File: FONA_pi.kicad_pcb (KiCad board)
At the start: 2 copper layers, 88.4 x 59.1 mm, 35 parts, among them J1 Conn_01x20_Socket, J10 Conn_01x04_Pin, J11 Conn_01x20_Socket, J12 Conn_01x20_Socket, J13 Conn_01x06_Socket, J14 Conn_01x06_Socket, J15 Conn_01x06_Socket, J17 Conn_01x06_Socket, J18 Conn_01x04, J2 Conn_02x20_Odd_Even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

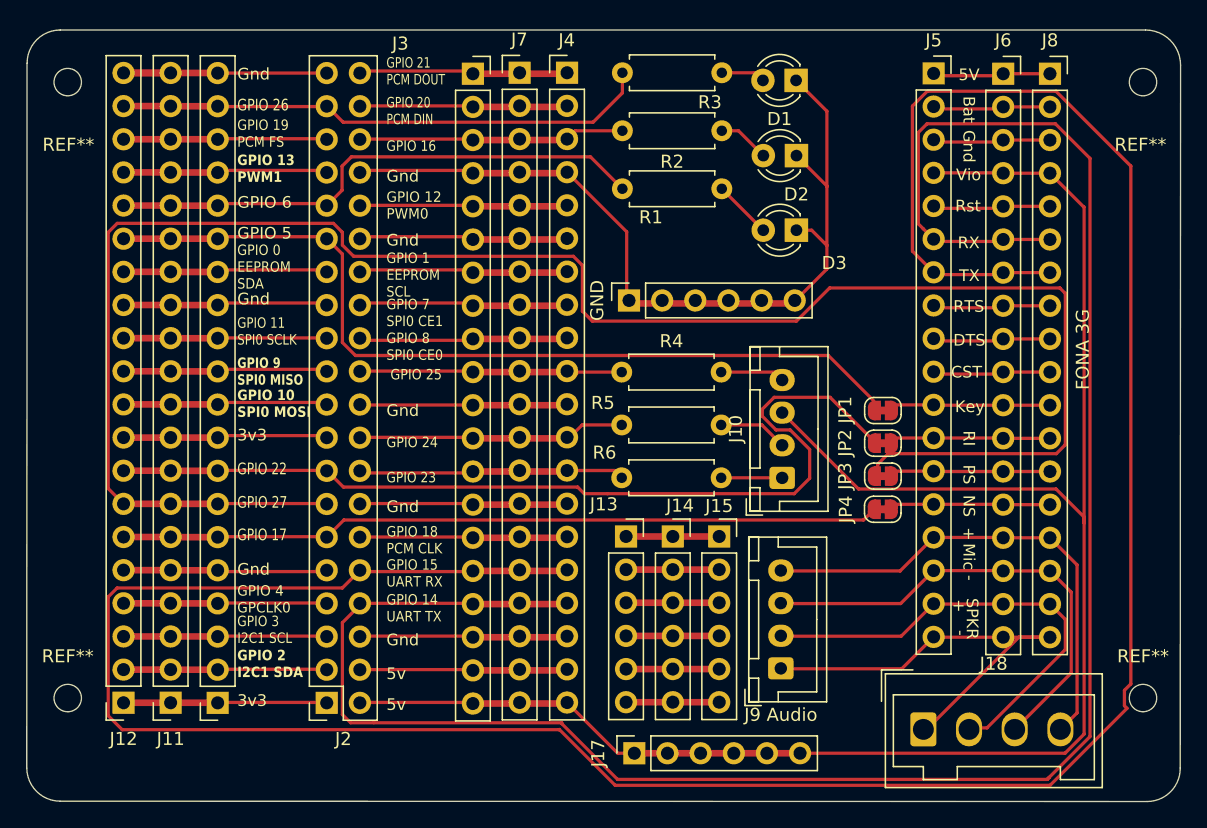
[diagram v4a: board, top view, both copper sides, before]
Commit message: Moved TX RX and +5V tracks to B.Cu
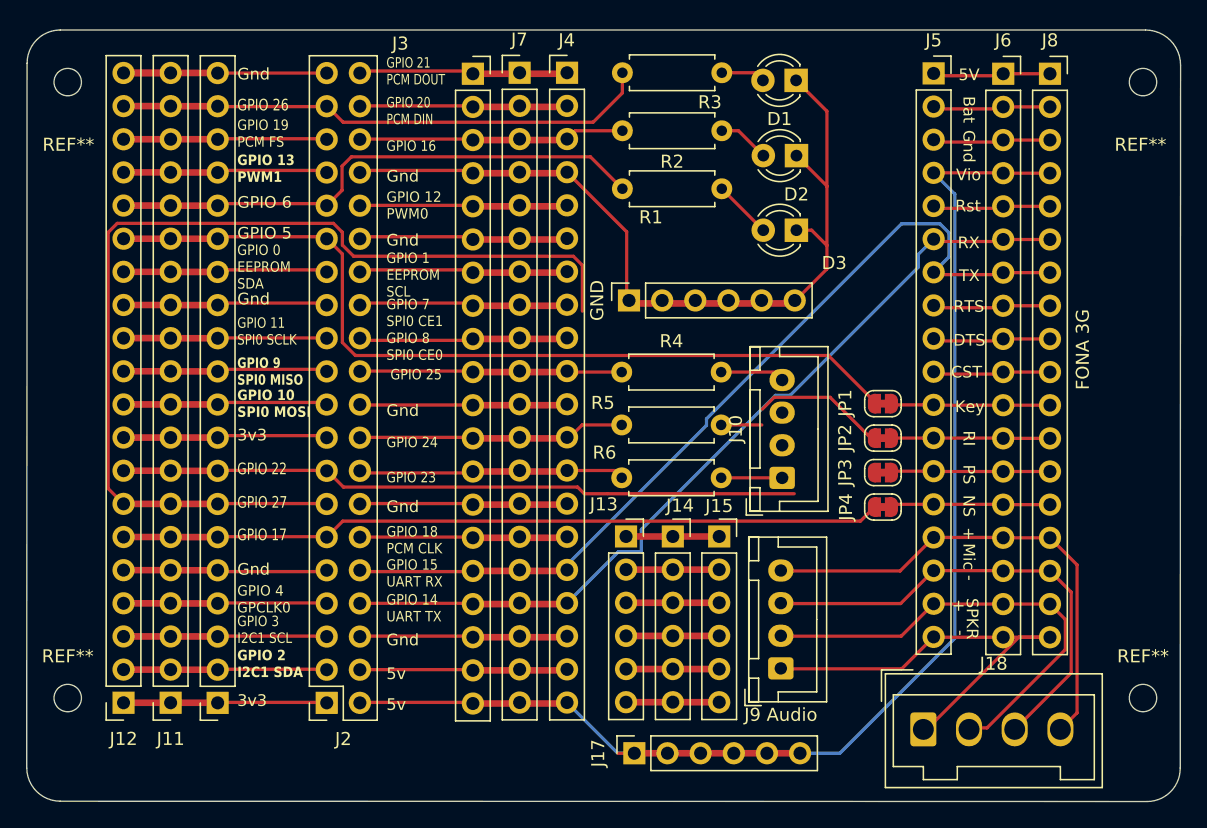
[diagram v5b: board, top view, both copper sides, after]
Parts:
- moved JP1 0.53 mm to (144.1, 86.2)
- moved JP2 0.39 mm to (144.1, 88.9)
- moved JP3 0.27 mm to (144.1, 91.5)
- moved JP4 0.17 mm to (144.1, 94.2)
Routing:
- net Net-(J2-Pin_10): track 210.8 -> 68.8 mm
- net Net-(J2-Pin_8): track 161.6 -> 65.3 mm
- net Net-(J1-Pin_7): track 144.7 -> 79.6 mm
- net Net-(J10-Pin_3): track 137.6 -> 97.4 mm
- net Net-(J1-Pin_8): track 71.8 -> 62.7 mm
- net Net-(J10-Pin_2): track 5.32 -> 3.12 mm
- net Net-(J5-Pin_14): track 12.3 -> 11.8 mm

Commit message: Re-routed tracks for the solder pads to more direct route to RPi
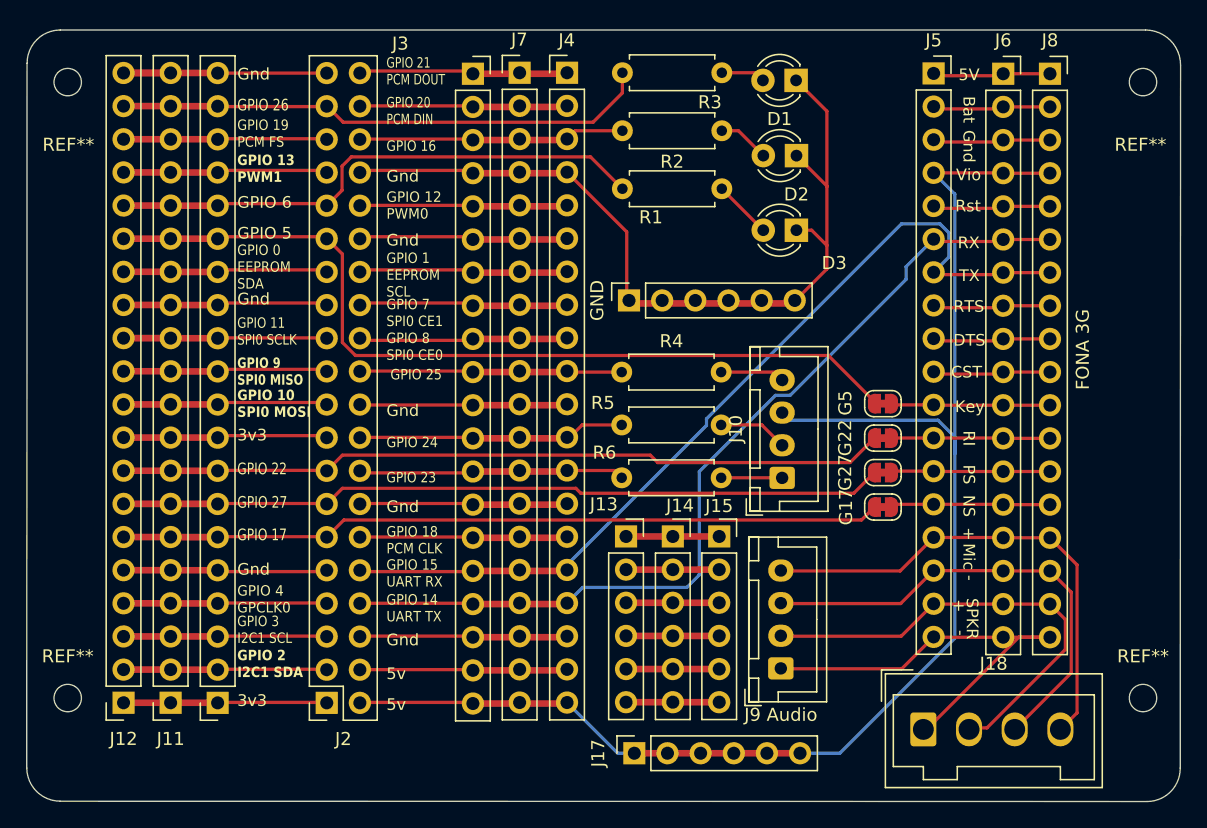
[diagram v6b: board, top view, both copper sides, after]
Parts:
- renumbered JP4 to G17, JP2 to G22, JP3 to G27, JP1 to G5
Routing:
- net Net-(J1-Pin_7): track 79.6 -> 59.1 mm
- net Net-(J10-Pin_3): track 97.4 -> 111.4 mm
- net Net-(J2-Pin_8): track 65.3 -> 68.9 mm
- net Net-(J1-Pin_8): track 62.7 -> 59.3 mm
- net Net-(J10-Pin_2): track 3.12 -> 5.32 mm
- net Net-(J2-Pin_10): track 68.8 -> 68.2 mm

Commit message: Had to place components from the schematic that I had already been placed (?).  Update PCB is fine from this point
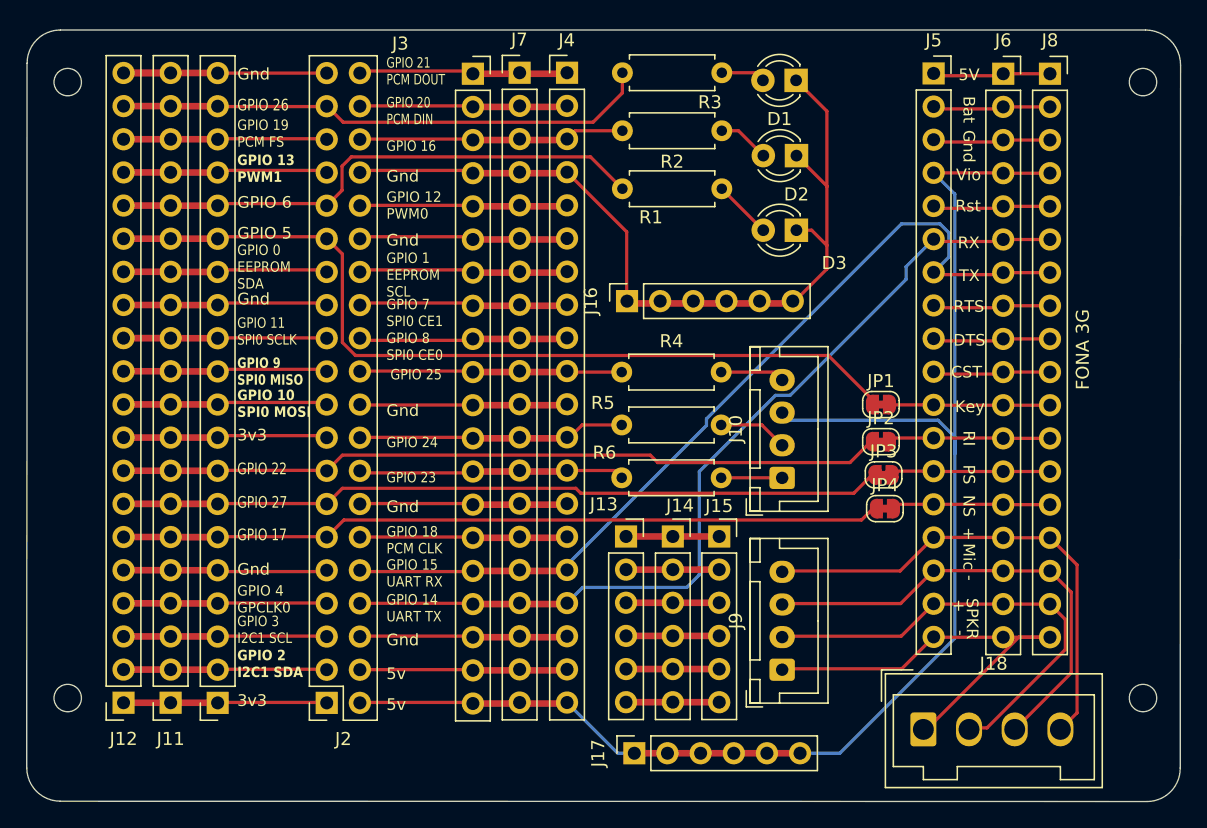
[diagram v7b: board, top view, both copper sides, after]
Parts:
- removed G17, G22, G27, G5: J2B, Jumper:SolderJumper-2_P1.3mm_Bridged_RoundedPad1.0x1.5mm
- removed GND: Conn_01x06_Socket, Connector_PinSocket_2.54mm:PinSocket_1x06_P2.54mm_Vertical
- removed J9 Audio: Conn_01x04_Pin, Connector_JST:JST_XH_B4B-XH-A_1x04_P2.50mm_Vertical
- added J16: Conn_01x06_Socket, Connector_PinSocket_2.54mm:PinSocket_1x06_P2.54mm_Vertical, F.Cu at (124.5, 78.4)
- added J9: Conn_01x04_Pin, Connector_JST:JST_XH_B4B-XH-A_1x04_P2.50mm_Vertical, F.Cu at (136.3, 106.6)
- added JP1: J2B, Jumper:SolderJumper-2_P1.3mm_Bridged_RoundedPad1.0x1.5mm, F.Cu at (143.9, 86.3)
- added JP2: J2B, Jumper:SolderJumper-2_P1.3mm_Bridged_RoundedPad1.0x1.5mm, F.Cu at (143.9, 89.2)
- added JP3: J2B, Jumper:SolderJumper-2_P1.3mm_Bridged_RoundedPad1.0x1.5mm, F.Cu at (144.1, 91.7)
- added JP4: J2B, Jumper:SolderJumper-2_P1.3mm_Bridged_RoundedPad1.0x1.5mm, F.Cu at (144.2, 94.3)
